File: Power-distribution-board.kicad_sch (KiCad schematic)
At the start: 89 parts, among them J1 178.6165.0001 breaker, J10 2606-1104/020-000, J12 2606-1104/020-000, J13 2606-1104/020-000, J15 2606-1104/020-000, J16 2606-1104/020-000, J2 178.6165.0001 breaker, J3 178.6165.0001 breaker, J4 178.6165.0001 breaker, J5 178.6165.0001 breaker, J6 178.6165.0001 breaker, J7 Screw_Terminal_01x03, J9 USB_C_Receptacle_USB2.0_14P, SW1 SW_Nidec_CAS-120A1, U1 ESP32-S3-WROOM-1, U11 TJA1051TK-3, U12 INA220BIDGSR, U13 INA220BIDGSR, U14 INA220BIDGSR, U15 INA220BIDGSR, U16 INA220BIDGSR, U17 INA220BIDGSR, U18 CP2102N-Axx-xQFN24, U2 LM3940IT-3.3, U3 INA220BIDGSR, U4 LM317_SOT-223, U5 TM1637, U6 CC56-12EWA

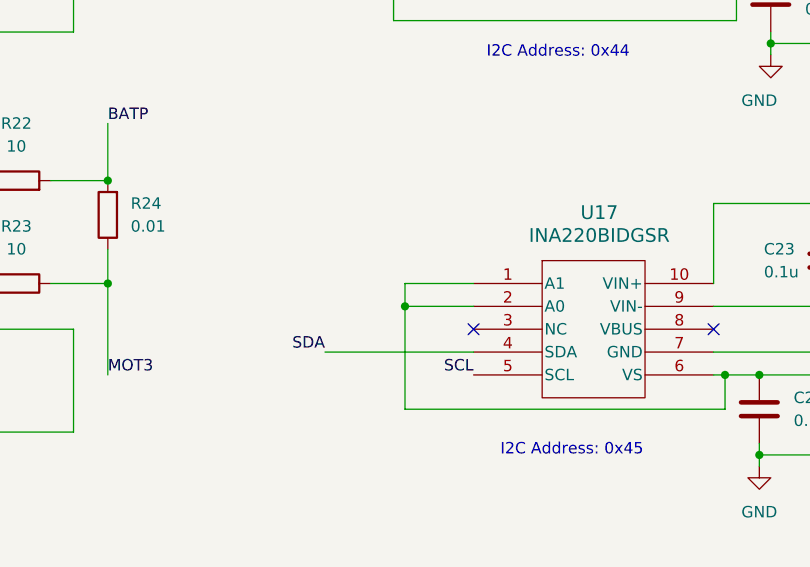
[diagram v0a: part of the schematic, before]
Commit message: fixed design rules errors
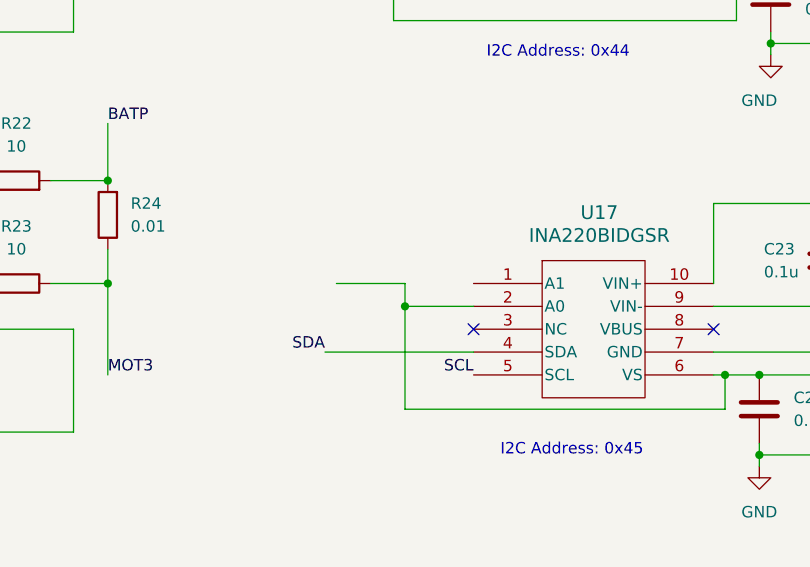
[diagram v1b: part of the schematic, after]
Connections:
- net 5V: no longer U17.1 (A1)
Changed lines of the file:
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@@
 	(wire
 		(pts
-			(xy 148.59 317.5) (xy 156.21 317.5)
+			(xy 148.59 317.5) (xy 140.97 317.5)
 		)
 		(stroke

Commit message: schematic changes from austen
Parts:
- added J8: 178.6165.0001, CONN_178.6165.0001_LTF, symbol PDB_symbols:178.6165.0001
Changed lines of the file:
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@@
+	)
+	(symbol
+		(lib_id "PDB_symbols:178.6165.0001")
+		(at 198.12 88.9 0)
+		(unit 1)
+		(exclude_from_sim no)
+		(in_bom yes)
+		(on_board yes)
+		(dnp no)
+		(fields_autoplaced yes)
+		(property "Reference" "J8"
+			(at 212.09 96.5199 0)
+			(effects
+				(font
+					(size 1.524 1.524)
+				)
+				(justify left)
+			)
+		)
+		(property "Value" "178.6165.0001"
+			(at 212.09 99.0599 0)
+			(effects
+				(font
+					(size 1.524 1.524)
+				)
+				(justify left)
+			)
+		)
+		(property "Footprint" "CONN_178.6165.0001_LTF"
+			(at 198.12 88.9 0)
+			(effects
+				(font
+					(size 1.27 1.27)
+					(italic yes)
+				)
+				(hide yes)
+			)
+		)
+		(property "Datasheet" "178.6165.0001"
+			(at 198.12 88.9 0)
+			(effects
+				(font
+					(size 1.27 1.27)
+					(italic yes)
+				)
+				(hide yes)
+			)
+		)
+		(property "Description" ""
+			(at 198.12 88.9 0)
+			(effects
+				(font
+					(size 1.27 1.27)
+				)
+				(hide yes)
+			)
+		)
+		(pin "6"
+		)
+		(pin "4"
+		)
+		(pin "5"
+		)
+		(pin "3"
+		)
+		(pin "1"
+		)
+		(pin "2"
+		)
+		(pin "7"
+		)
+		(pin "8"
+		)
+		(instances
+			(project ""
+				(path "/99d8dfce-413e-440e-9a66-3580ccaf9f1d"
+					(reference "J8")
+					(unit 1)
+				)
+			)
+		)
 	)
 	(symbol

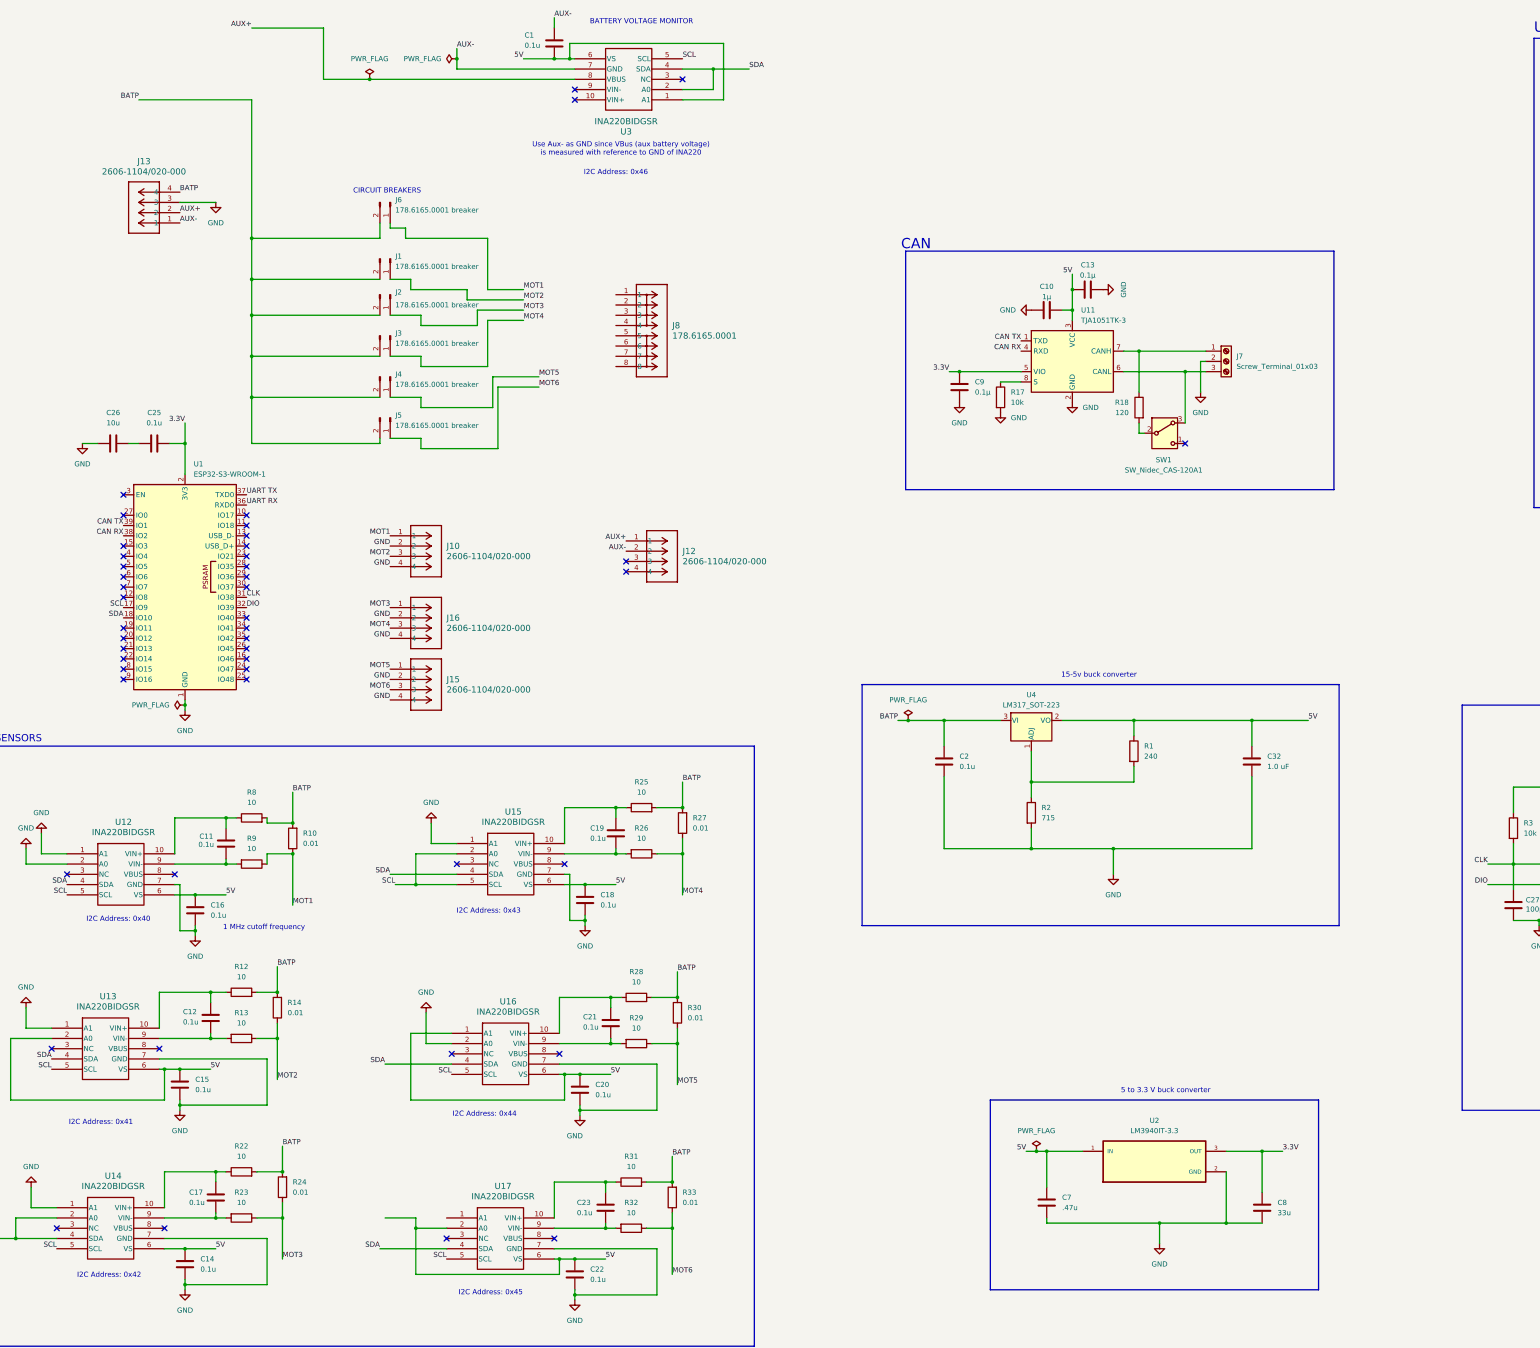
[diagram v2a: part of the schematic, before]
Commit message: redid layout
implemented some of austens advice. changes:
- correct symbol and footprint used for fuse holders
- correct orientation of usb port
- more compact design?
- placement of current sensors is closer to their respective motor connections
- pwr planes utilize whole board space for heat dissipation

notes -
- need help doing traces. need to figure out how to trace to treat high current optimally
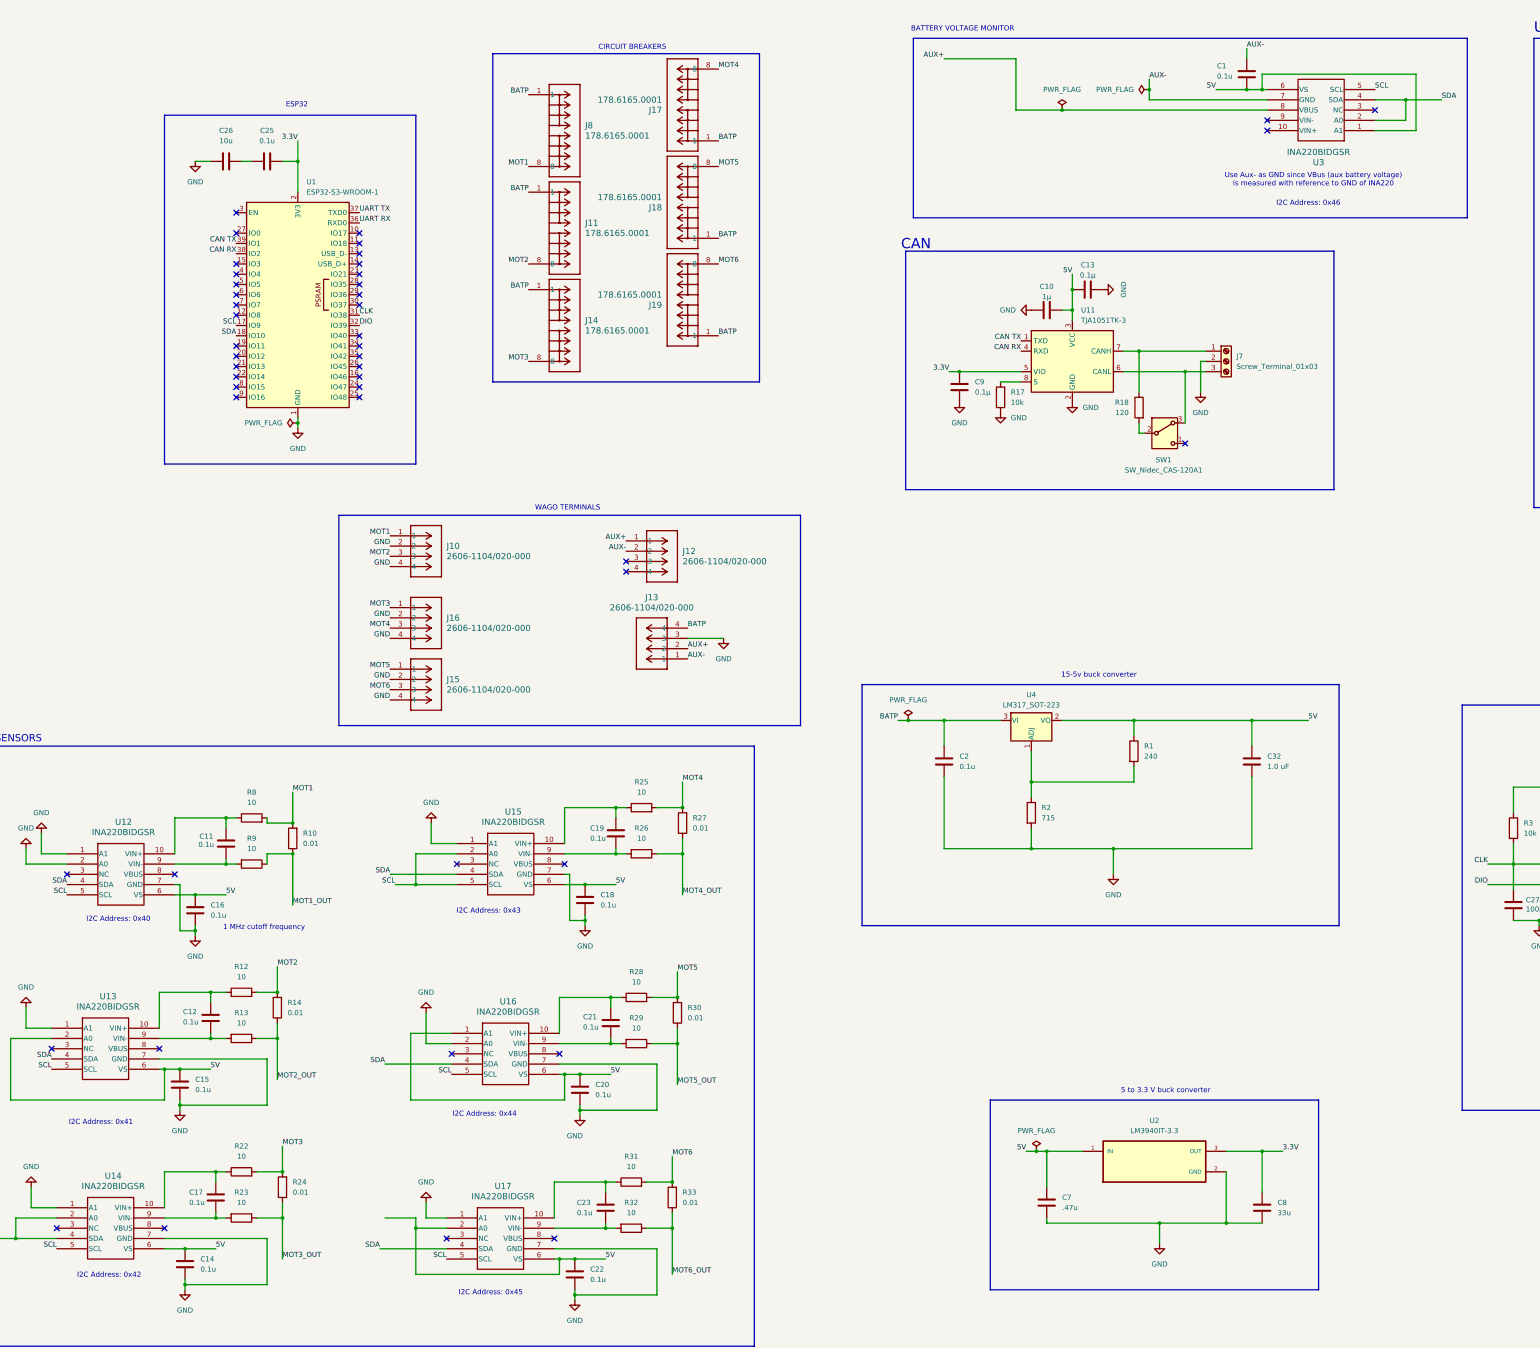
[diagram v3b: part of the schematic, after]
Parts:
- removed J1, J2, J3, J4, J5, J6: 178.6165.0001 breaker, pdb_footprints:CONN_178.6165.0001_LTF, symbol Connector:Conn_01x02_Pin
- added J11, J14, J17, J18, J19: 178.6165.0001, CONN_178.6165.0001_LTF, symbol PDB_symbols:178.6165.0001
- U5: footprint pdb_footprints:LED_driver_TM1637 -> TM1637:DIP778W43P254L2612H431Q20N
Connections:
- net BATP: now also J8.1, J11.1, J14.1, J17.1, J18.1, J19.1; no longer R10.2, R12.2, R14.2, R22.2, R24.2, R25.2, R27.2, R28.2, R30.2, R31.2, R33.2, R8.2
- net GND: now also U17.1 (A1)
- net MOT1: now also J8.8, R10.2, R8.2; no longer R10.1, R9.1
- net MOT2: now also R12.2, R14.2, J11.8; no longer R13.1, R14.1
- net MOT3: now also R22.2, R24.2, J14.8; no longer R23.1, R24.1
- net MOT4: now also R25.2, R27.2, J17.8; no longer R26.1, R27.1
- net MOT5: now also R28.2, R30.2, J18.8; no longer R29.1, R30.1
- net MOT6: now also R31.2, R33.2, J19.8; no longer R32.1, R33.1
- new net MOT1_OUT: R10.1, R9.1
- new net MOT2_OUT: R13.1, R14.1
- new net MOT3_OUT: R23.1, R24.1
- new net MOT4_OUT: R26.1, R27.1
- new net MOT5_OUT: R29.1, R30.1
- new net MOT6_OUT: R32.1, R33.1
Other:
- note added: "ESP32"
- note added: "WAGO TERMINALS"
- moved on the sheet: C1, C25, C26, J13, U1, U3

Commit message: cleaned up repo
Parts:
- removed U4: LM317_SOT-223, Package_TO_SOT_SMD:SOT-223-3_TabPin2, symbol Regulator_Linear:LM317_SOT-223
- added U7: LM317_SOT-223, Package_TO_SOT_SMD:SOT-223-3_TabPin2, symbol Regulator_Linear:LM317_SOT-223
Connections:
- net 3.3V: now also C26.2
- net 5V: now also C13.1, U7.2 (VO); no longer C13.2
- net BATP: now also U7.3 (VI)
- net GND: now also C13.2, C25.1; no longer C13.1, J10.2, J10.4, J13.3, J15.2, J15.4, J16.2, J16.4
- net at R1.2, R2.1: now also U7.1 (ADJ)
- new net BATN: J10.2, J10.4, J13.3, J15.2, J15.4, J16.2, J16.4
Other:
- moved on the sheet: C13, C25, C26, J10, J11, J12, J13, J14, J15, J16, J17, J18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

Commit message: Fixed schematic
-shunt resistor changed to 0.1mO that can handle 8W
-change R10 values to R0 in current sensing circuit
-flip gnd down (convention)
-CAN: get rid of switch; replace with short
-new buck converter for 15v-5v instead of LDO
-updated footprints
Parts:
- removed C2: 0.1u, Capacitor_SMD:C_0805_2012Metric, symbol Device:C
- removed C32: 1.0 uF, Capacitor_SMD:C_0805_2012Metric, symbol Device:C
- removed R1: 240, Resistor_SMD:R_0805_2012Metric, symbol Device:R
- removed R2: 715, Resistor_SMD:R_0805_2012Metric, symbol Device:R
- removed SW1: SW_Nidec_CAS-120A1, Button_Switch_SMD:Nidec_Copal_CAS-120A, symbol Switch:SW_Nidec_CAS-120A1
- removed U7: LM317_SOT-223, Package_TO_SOT_SMD:SOT-223-3_TabPin2, symbol Regulator_Linear:LM317_SOT-223
- added 15-5VRM1: TPS62933DRLR, PDB Footprint Library:SOT-5X3-8_DRL_TEX, symbol powerdist:TPS62933DRLR
- added C24, C31: 10uF, PDB Footprint Library:CAP_CGA5_TDK-M, symbol Device:C
- added C33, C35, C38: 100nF, Capacitor_SMD:C_0402_1005Metric, symbol Device:C
- added C34: 33nF, Capacitor_SMD:C_0402_1005Metric, symbol Device:C
- added C36, C37: 22uF, Capacitor_SMD:C_0805_2012Metric, symbol Device:C
- added J1: Conn_01x03_Pin, Connector_PinHeader_1.00mm:PinHeader_1x03_P1.00mm_Vertical_SMD_Pin1Left, symbol Connector:Conn_01x03_Pin
- added L1: 6.8uH, Inductor_SMD:L_Wuerth_XHMI-6060, symbol Device:L
- added R11: 511k, Resistor_SMD:R_0805_2012Metric, symbol Device:R
- added R15: 88.7k, Resistor_SMD:R_0805_2012Metric, symbol Device:R
- added R19: 10.2k, Resistor_SMD:R_0805_2012Metric, symbol Device:R
- added R20: 0, Resistor_SMD:R_0805_2012Metric, symbol Device:R
- added R21: 53.55k, Resistor_SMD:R_0805_2012Metric, symbol Device:R
- added R34: 49.9, Resistor_SMD:R_0805_2012Metric, symbol Device:R
- J11, J14, J17, J18, J19, J8: footprint CONN_178.6165.0001_LTF -> PDB Footprint Library:CONN_178.6165.0001_LTF
- R10, R14, R24, R27, R30, R33: value 0.01 -> 1m; footprint Resistor_SMD:R_0805_2012Metric -> PDB Footprint Library:RES_3920R_1L00x_BRN-M
- R12, R13, R22, R23, R25, R26, R28, R29, R31, R32, R8, R9: value 10 -> 0
- U2: footprint pdb_footprints:T03B -> PDB Footprint Library:T03B
- U5: footprint TM1637:DIP778W43P254L2612H431Q20N -> PDB Footprint Library:LED_driver_DIP778W43P254L2612H431Q20N
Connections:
- net 5V: now also U17.1 (A1), C36.1, C37.1, C38.1, L1.2, R34.1
- net BATP: now also 15-5VRM1.3 (VIN), C24.1, C31.1, C33.1, R11.2
- net GND: now also 15-5VRM1.4 (GND), C24.2, C31.2, C33.2, C34.2, C36.2, C37.2, C38.2, J1.1 (Pin_1), R15.1, R19.1; no longer U17.1 (A1)
- net at J7.3 (Pin_3), U11.6 (CANL): now also R18.2
- new net: J1.3 (Pin_3), R11.1, R15.2
- new net: 15-5VRM1.8 (FB), R19.2, R21.1, R21.2, R34.2
- new net: 15-5VRM1.5 (SW), C35.2, L1.1
- new net: C35.1, R20.1
- new net: 15-5VRM1.6 (BST), R20.2
- new net: 15-5VRM1.2 (EN), J1.2 (Pin_2)
- new net: 15-5VRM1.7 (SS), C34.1
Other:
- note added: "15V-5V Buck Converter"
- note added: "5 to 3.3 V Step-down LDO"
- note removed: "15-5v buck converter"
- note removed: "5 to 3.3 V buck converter"
- company: (none) -> MARS
- title: (none) -> Lunabotics Power Distribution Board
- moved on the sheet: C1, C10, C11, C12, C13, C14, C15, C16, C17, C18, C19, C20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

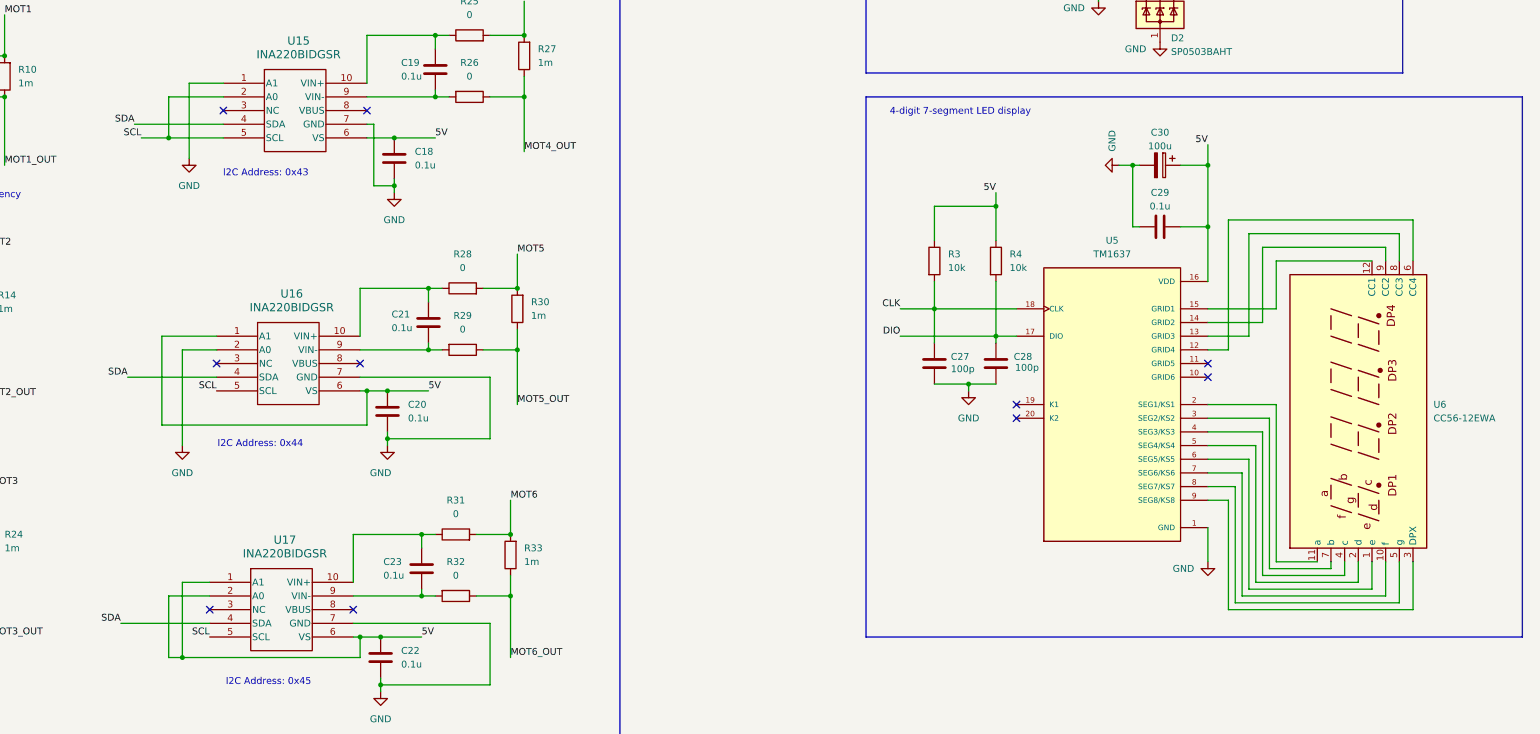
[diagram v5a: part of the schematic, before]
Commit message: update schematic and pcb
- add pull up resistors for sda and scl
- added buck converter to pcb layout
- batp & batn planes top and bottom
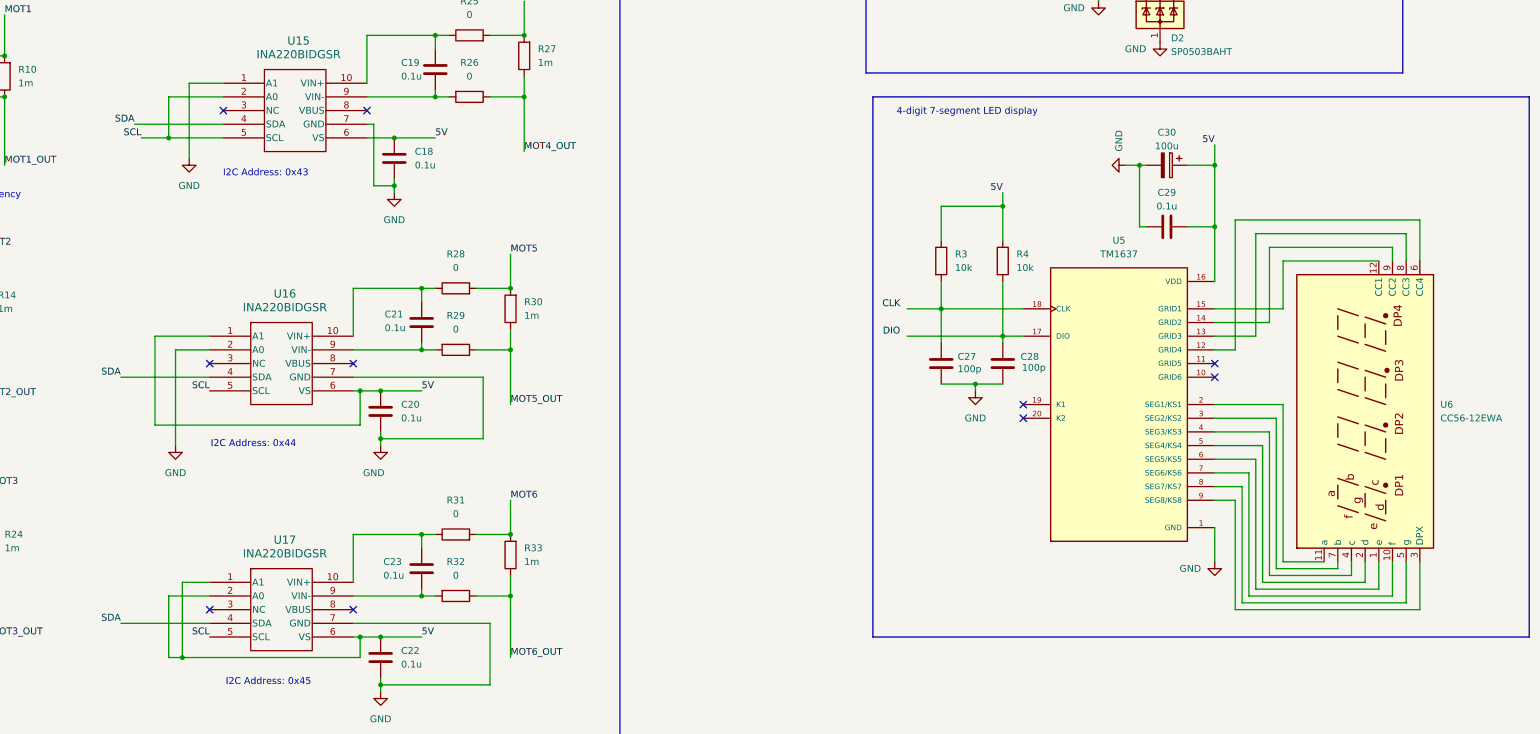
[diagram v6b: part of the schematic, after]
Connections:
- net CLK: no longer C27.2, R3.2, U5.18 (CLK)
- net DIO: no longer C28.1, R4.2, U5.17 (DIO)
- new net: C28.1, R4.2, U5.17 (DIO)
- new net: C27.2, R3.2, U5.18 (CLK)
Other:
- moved on the sheet: C20, C21, C27, C28, C29, C30, R28, R29, R3, R30, R4, U16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
